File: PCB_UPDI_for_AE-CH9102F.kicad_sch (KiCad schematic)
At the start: 8 parts, among them J1 AE-CH9102F, J2 UPDI, J3 TTL Serial, J4 RTS / DTR, SW1 UPDI / Serial, SW2 Power

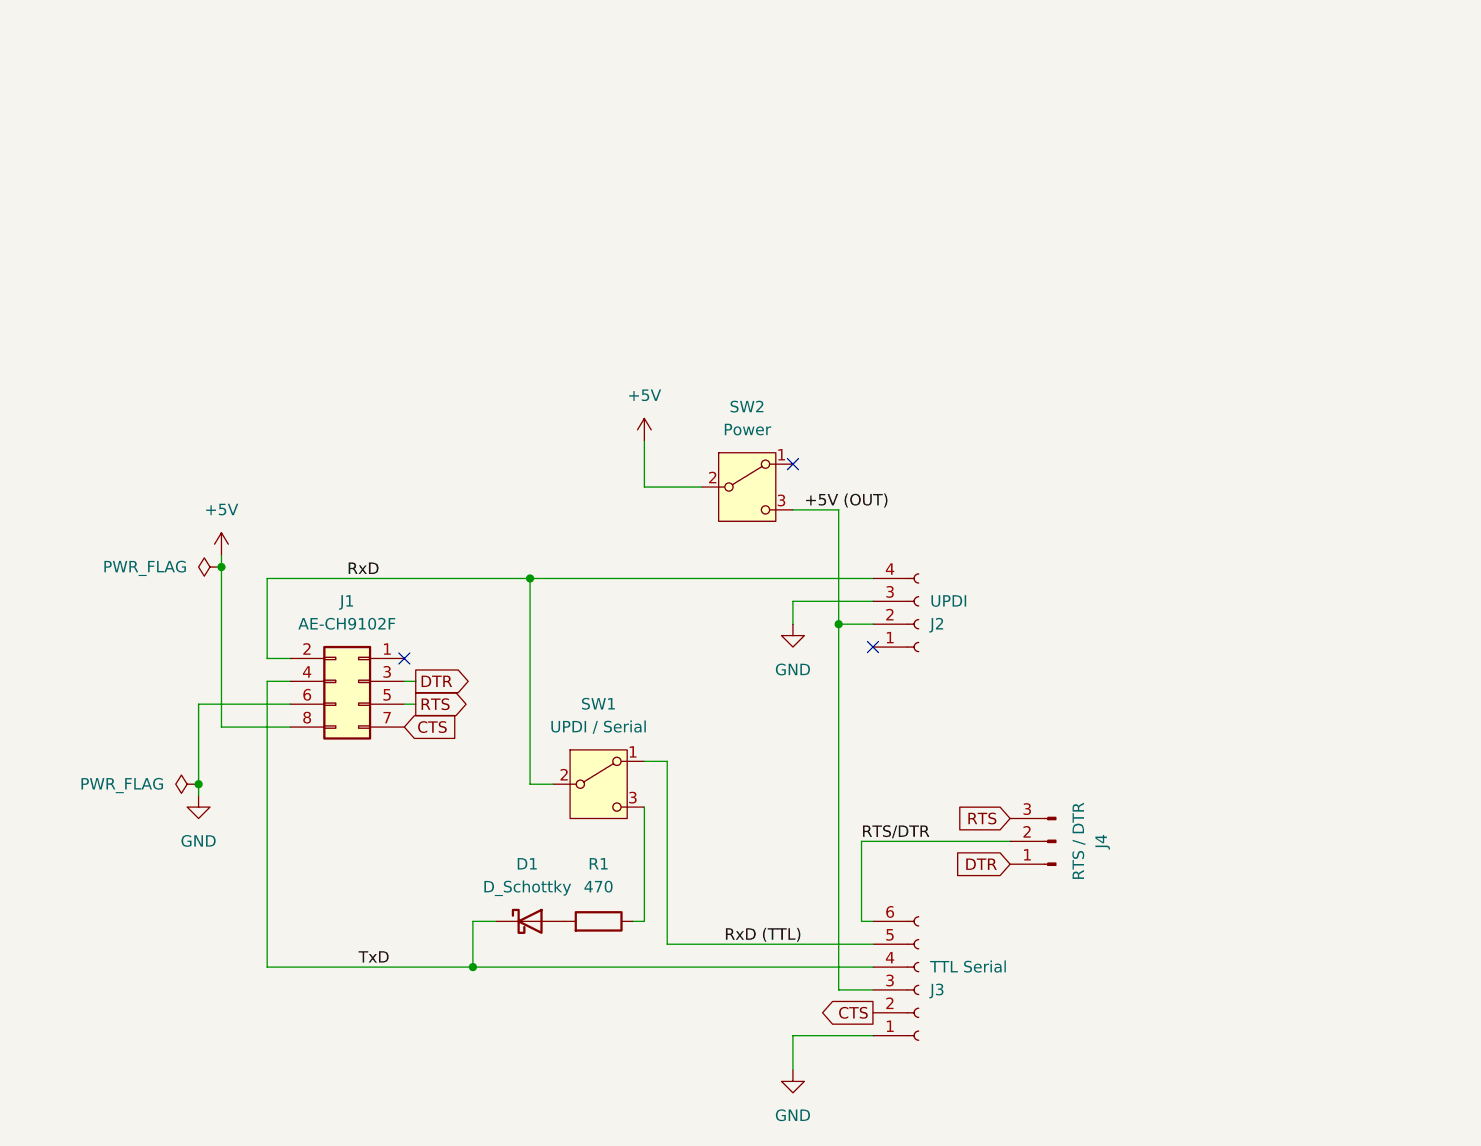
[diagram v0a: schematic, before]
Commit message: Rev. 2
Implement auto switching between the UPDI mode and the UART mode.
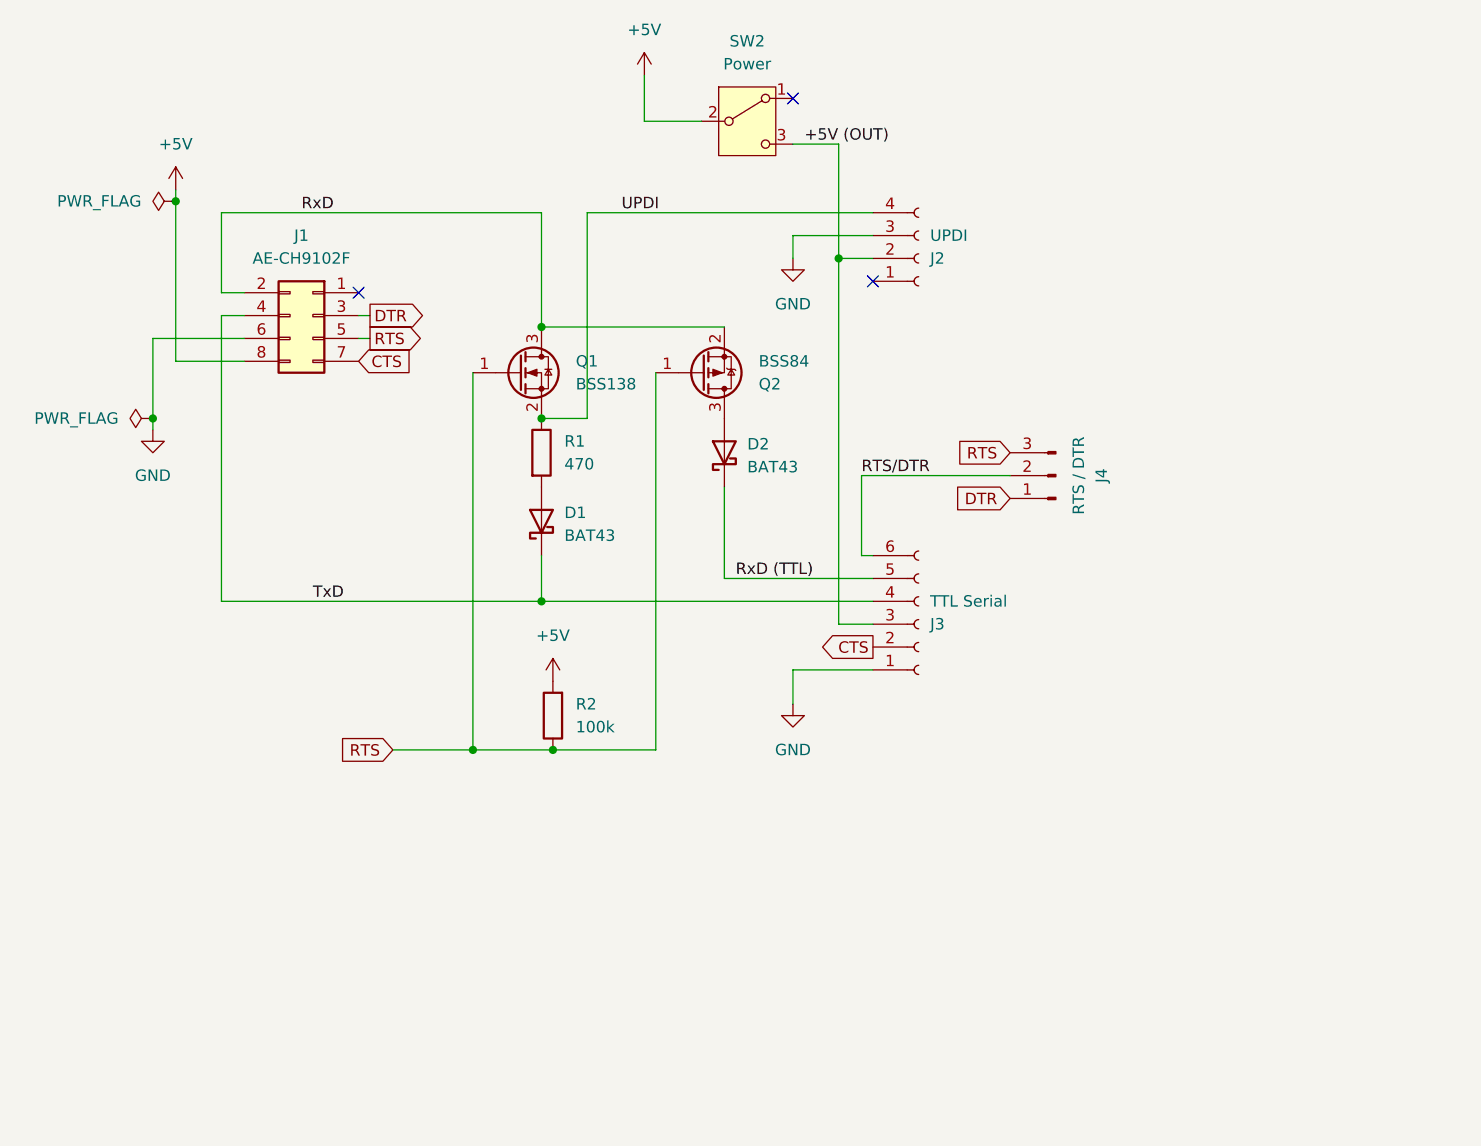
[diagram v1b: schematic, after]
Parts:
- removed D1: D_Schottky, Diode_THT:D_A-405_P2.54mm_Vertical_KathodeUp, symbol Device:D_Schottky
- removed SW1: UPDI / Serial, Connector_PinHeader_2.54mm:PinHeader_1x03_P2.54mm_Vertical, symbol Switch:SW_SPDT
- added D1, D2: BAT43, Diode_THT:D_DO-35_SOD27_P2.54mm_Vertical_KathodeUp, symbol Diode:BAT43
- added Q1: BSS138, Package_TO_SOT_SMD:SOT-23, symbol Transistor_FET:BSS138
- added Q2: BSS84, Package_TO_SOT_SMD:SOT-23, symbol Transistor_FET:BSS84
- added R2: 100k, Resistor_THT:R_Axial_DIN0204_L3.6mm_D1.6mm_P2.54mm_Vertical, symbol Device:R
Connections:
- net +5V: now also R2.2
- net RTS: now also Q1.1 (G), Q2.1 (G), R2.1
- net RxD: now also Q1.3 (D), Q2.2 (S); no longer J2.4 (Pin_4)
- net RxD (TTL): now also D2.1 (K)
- net TxD: now also D1.1 (K)
- net UPDI: now reaches R1.1
- net UPDI: now also J2.4 (Pin_4), Q1.2 (S)
- net at R1.2: now also D1.2 (A)
- new net: D2.2 (A), Q2.3 (D)
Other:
- moved on the sheet: J1, J2, J3, J4, R1, SW2

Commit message: Update for Rev. 3
* Use 74LVC1G3157.
* Use SMD devices.
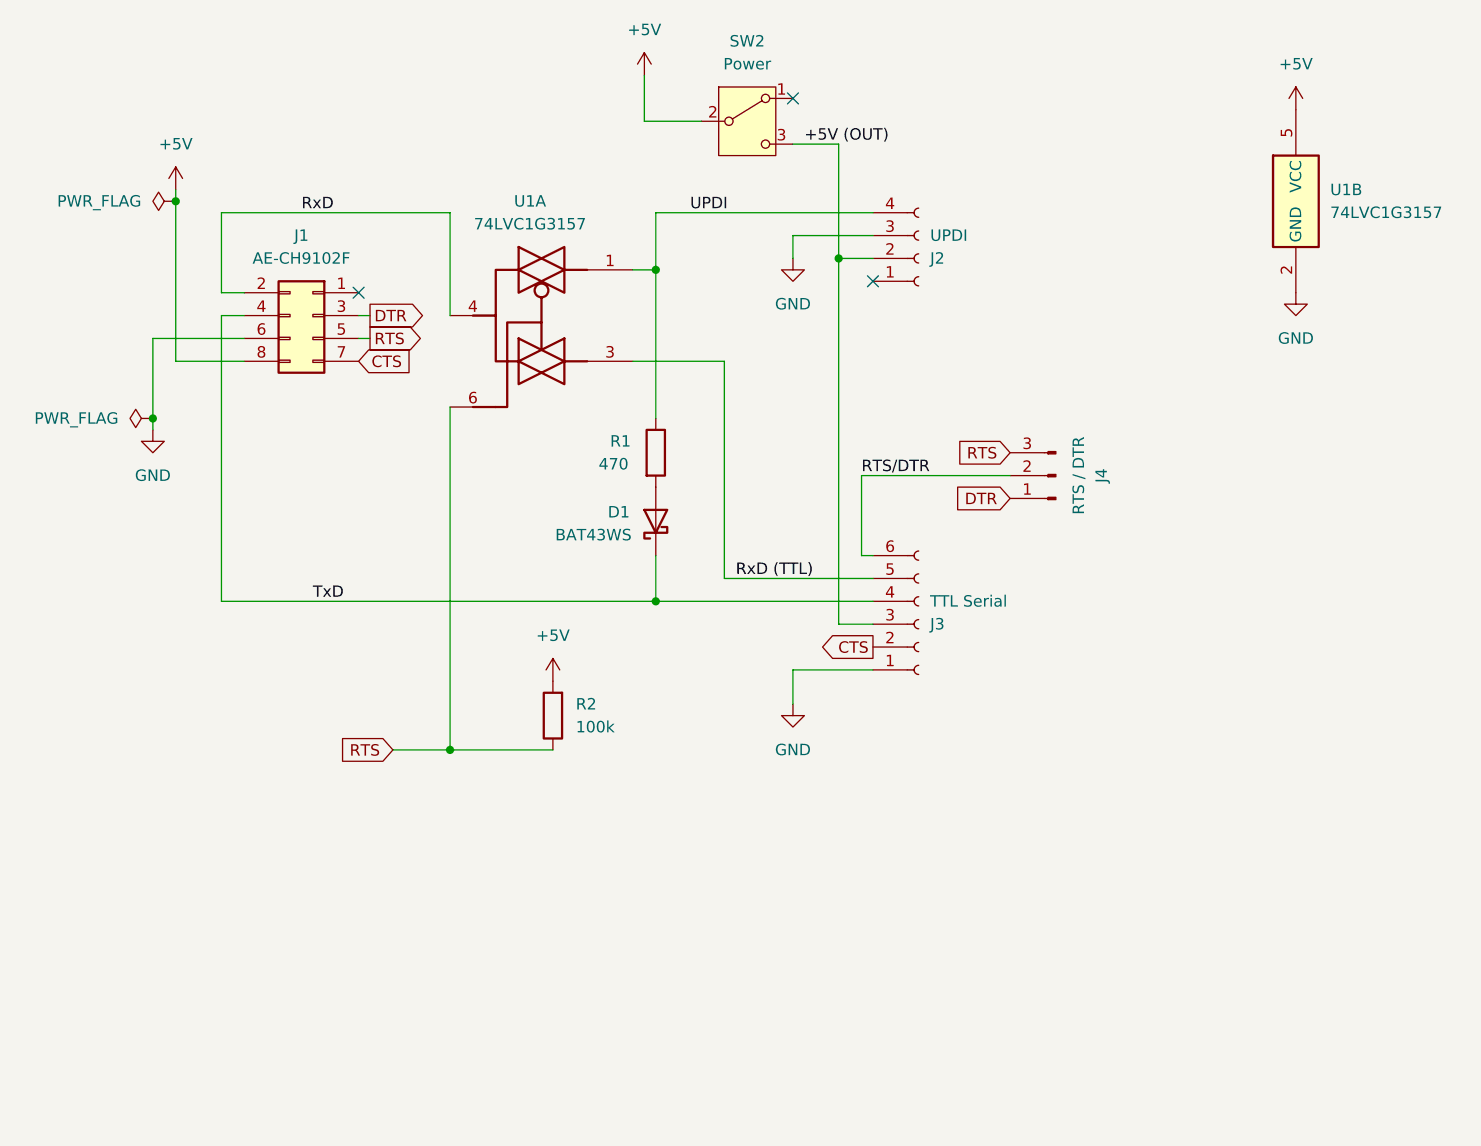
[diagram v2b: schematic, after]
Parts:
- removed D2: BAT43, Diode_THT:D_DO-35_SOD27_P2.54mm_Vertical_KathodeUp, symbol Diode:BAT43
- removed Q1: BSS138, Package_TO_SOT_SMD:SOT-23, symbol Transistor_FET:BSS138
- removed Q2: BSS84, Package_TO_SOT_SMD:SOT-23, symbol Transistor_FET:BSS84
- added U1: 74LVC1G3157, Package_TO_SOT_SMD:SOT-23-6, symbol 74xGxx:74LVC1G3157
- D1: value BAT43 -> BAT43WS; footprint Diode_THT:D_DO-35_SOD27_P2.54mm_Vertical_KathodeUp -> Diode_SMD:D_0603_1608Metric
- R1, R2: footprint Resistor_THT:R_Axial_DIN0204_L3.6mm_D1.6mm_P2.54mm_Vertical -> Resistor_SMD:R_0603_1608Metric
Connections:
- net +5V: now also U1.5 (VCC)
- net GND: now also U1.2 (GND)
- net RTS: now also U1.6
- net RxD: now also U1.4
- net RxD (TTL): now also U1.3
- net UPDI: now also U1.1
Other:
- moved on the sheet: D1, R1
